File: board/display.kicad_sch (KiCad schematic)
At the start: 2 parts

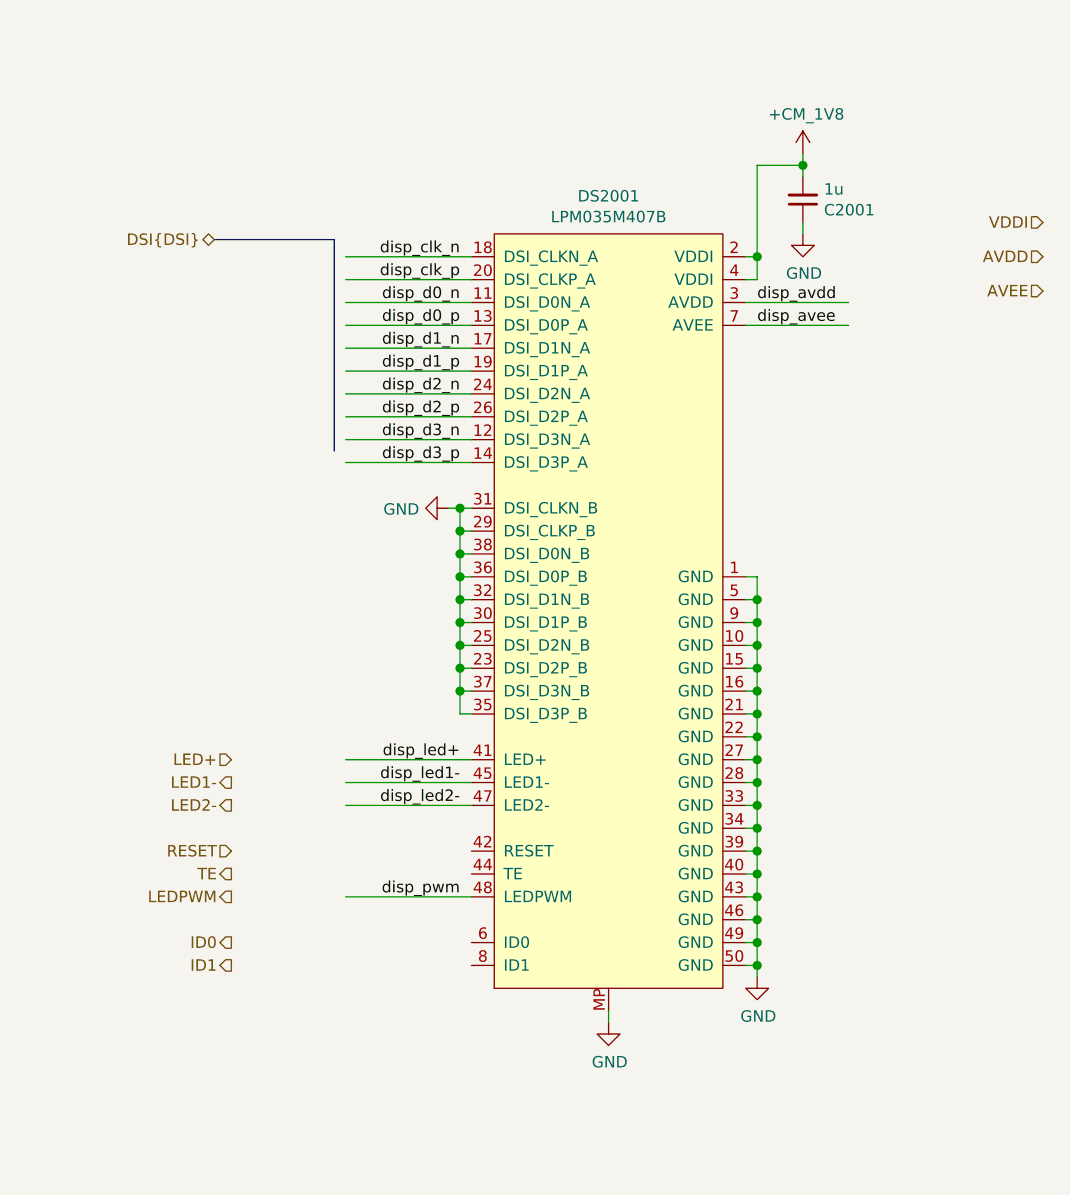
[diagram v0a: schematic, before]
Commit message: Added testpoints and other fixes
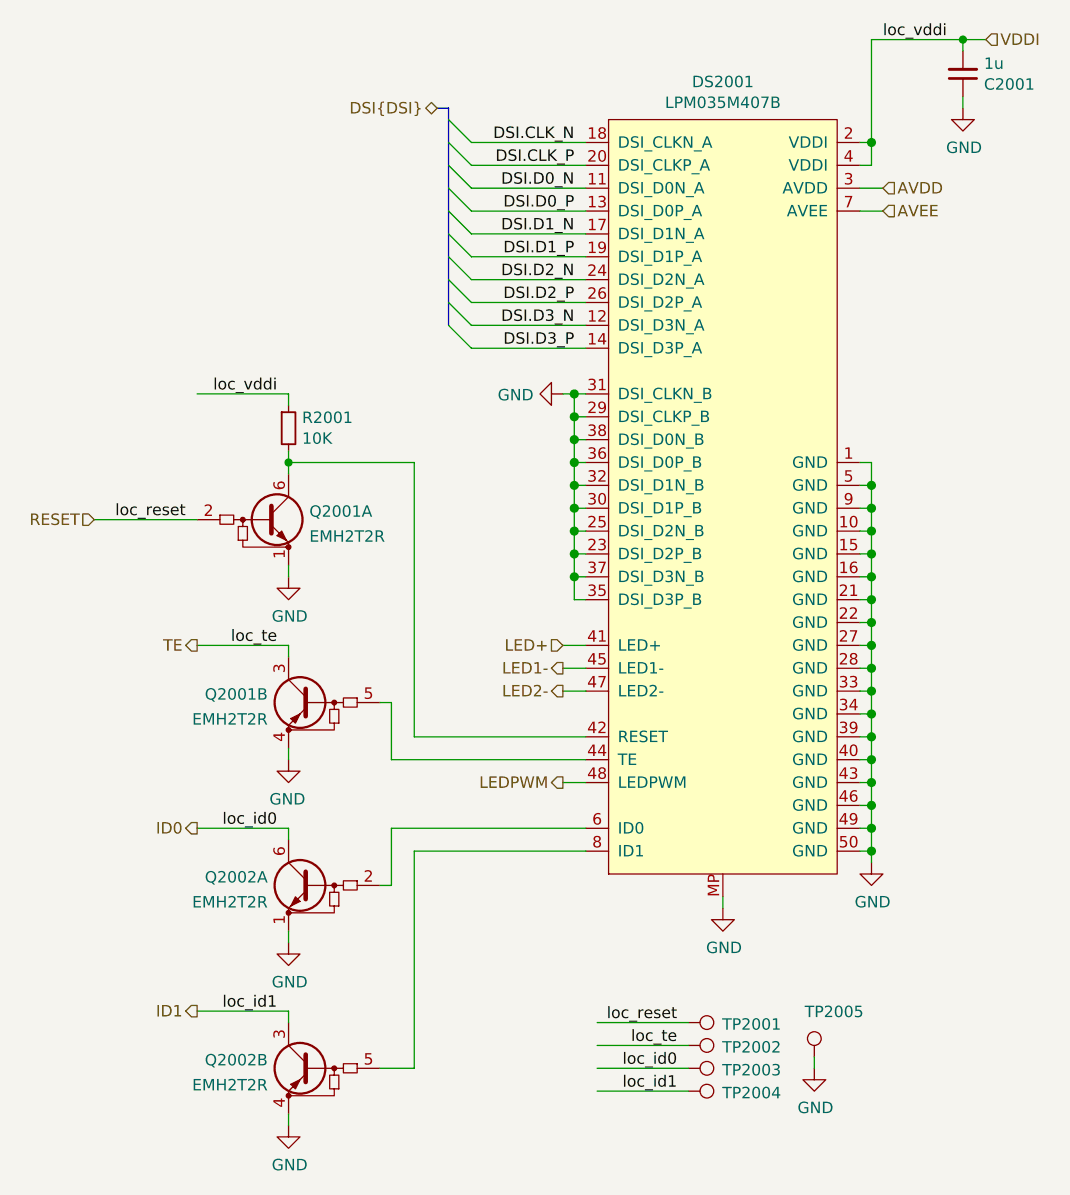
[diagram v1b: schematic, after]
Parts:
- added Q2001, Q2002: EMH2T2R, DIYPie:SOT-563, symbol DIYPie:EMH2T2R
- added R2001: 10K, DIYPie:R_0402_1005Metric, symbol Device:R_Small
- added TP2001, TP2002, TP2003, TP2004, TP2005: TestPoint, DIYPie:TestPoint_Pad_D1.5mm, symbol DIYPie:TestPoint
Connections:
- net +1V8 is gone; now on net VDDI: C2001.2, DS2001.2 (VDDI), DS2001.4 (VDDI)
- net disp_avdd is gone; now on net AVDD: DS2001.3 (AVDD)
- net disp_avee is gone; now on net AVEE: DS2001.7 (AVEE)
- net disp_led+ is gone; now on net LED+: DS2001.41 (LED+)
- net disp_led1- is gone; now on net LED1-: DS2001.45 (LED1-)
- net disp_led2- is gone; now on net LED2-: DS2001.47 (LED2-)
- net disp_pwm is gone; now on net LEDPWM: DS2001.48 (LEDPWM)
- net GND: now also Q2001.1 (E1), Q2001.4 (E1), Q2002.1 (E1), Q2002.4 (E1), TP2005.1
- net ID0: now also Q2002.6 (C1), TP2003.1
- net ID1: now also Q2002.3 (C1), TP2004.1
- net RESET: now also Q2001.2 (B1), TP2001.1
- net TE: now also Q2001.3 (C1), TP2002.1
- net VDDI: now also R2001.1
- net at DS2001.42 (RESET): now also Q2001.6 (C1), R2001.2
- net at DS2001.44 (TE): now also Q2001.5 (B1)
- net at DS2001.6 (ID0): now also Q2002.2 (B1)
- net at DS2001.8 (ID1): now also Q2002.5 (B1)
- net disp_clk_n renamed DSI.CLK_N
- net disp_clk_p renamed DSI.CLK_P
- net disp_d0_n renamed DSI.D0_N
- net disp_d0_p renamed DSI.D0_P
- net disp_d1_n renamed DSI.D1_N
- net disp_d1_p renamed DSI.D1_P
- net disp_d2_n renamed DSI.D2_N
- net disp_d2_p renamed DSI.D2_P
- net disp_d3_n renamed DSI.D3_N
- net disp_d3_p renamed DSI.D3_P
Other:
- moved on the sheet: C2001, DS2001
